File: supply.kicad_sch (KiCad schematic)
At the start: 57 parts, among them Q1 DMG1012T-7, Q3 DMG1012T-7, U1 AP62301_TSOT, U2 AP62301_TSOT, U3 NCP163ASN330T1G, U4 REF3012AIDBZT, U5 TLV73312PDBVT

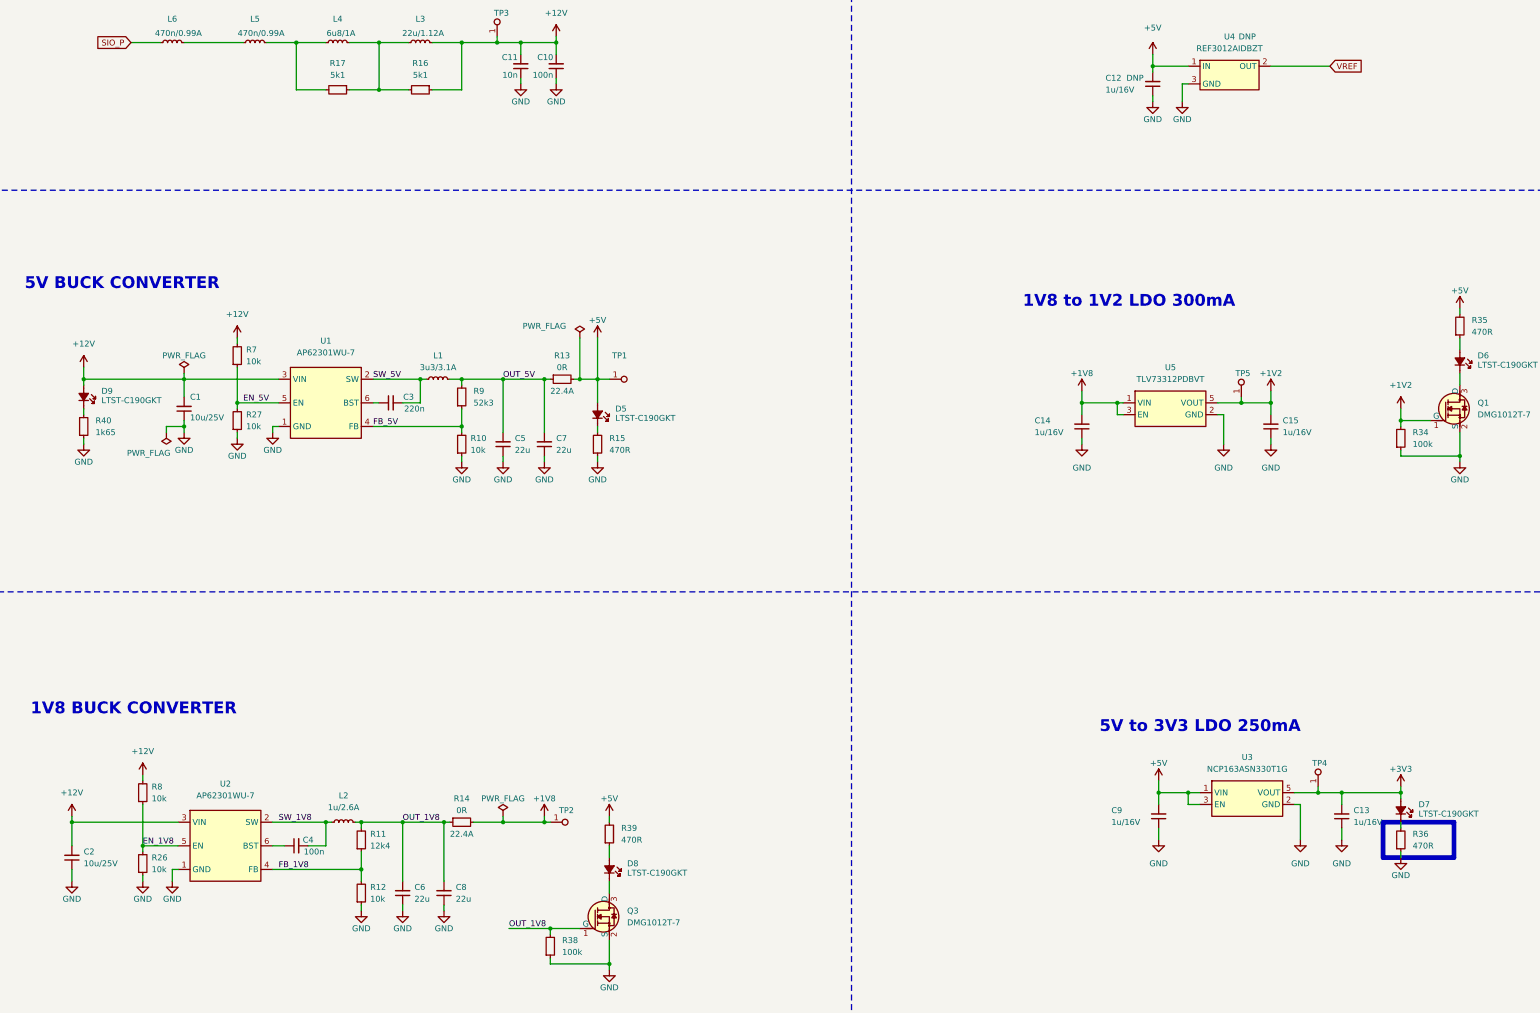
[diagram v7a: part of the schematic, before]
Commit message: [#55438] Place LED indicators on PCB
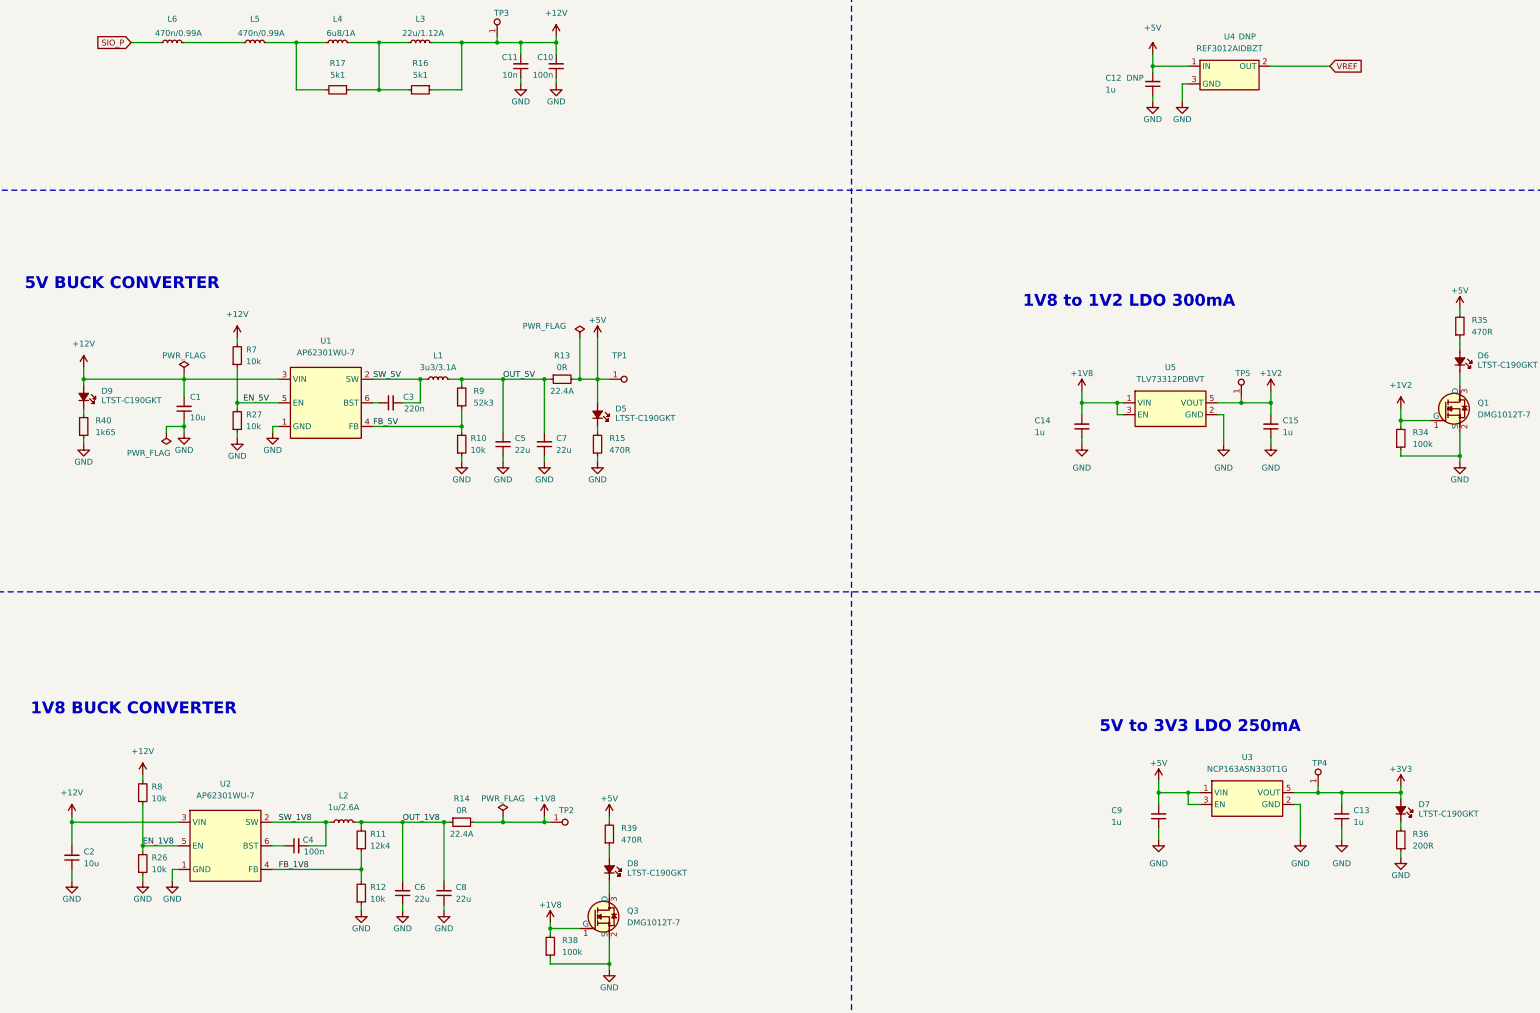
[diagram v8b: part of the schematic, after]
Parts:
- removed R36: R_470R_0402, antmicro-footprints:R_0402_1005Metric, symbol antmicroResistors0402:R_470R_0402
- added R36: R_200R_0402, antmicro-footprints:R_0402_1005Metric, symbol antmicroResistors0402:R_200R_0402
- C1, C2: Val 10u/25V -> 10u; Voltage (none) -> 25V
- C12, C13, C14, C15, C9: Val 1u/16V -> 1u; Voltage (none) -> 16V
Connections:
- net +1V8: now also Q3.1 (G), R38.2
- net GND: now also R36.1
- net OUT_1V8: no longer Q3.1 (G), R38.2
- net at D7.1 (C): now also R36.2
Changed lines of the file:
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@@
     (stroke (width 0) (type default))
   )
-  (wire (pts (xy 147.32 240.03) (xy 156.21 240.03))
-    (stroke (width 0) (type default))
-  )
   (wire (pts (xy 154.94 215.9) (xy 154.94 217.17))
     (stroke (width 0) (type default))
@@
     (stroke (width 0) (type default))
   )
+  (wire (pts (xy 156.21 238.76) (xy 156.21 240.03))
+    (stroke (width 0) (type default))
+  )
   (wire (pts (xy 101.6 49.53) (xy 107.95 49.53))
     (stroke (width 0) (type default))
@@
     (stroke (width 0) (type default))
   )
-  (rectangle (start 335.28 217.17) (end 350.52 224.79)
-    (stroke (width 1) (type default) (color 255 0 0 1))
-    (fill (type none))
-  )
   (image (at 35.56 274.32) (scale 0.4)
     (data
@@
     (effects (font (size 1.27 1.27)) (justify left bottom))
   )
-  (label "OUT_1V8" (at 147.32 240.03 0) (fields_autoplaced)
-    (effects (font (size 1.27 1.27)) (justify left bottom))
-  )
   (label "EN_5V" (at 90.17 127 0) (fields_autoplaced)
     (effects (font (size 1.27 1.27)) (justify left bottom))
@@
       (effects (font (size 1.27 1.27) (thickness 0.15)) (justify left bottom) hide)
     )
-    (property "Val" "1u/16V" (at 328.93 217.17 90)
+    (property "Val" "1u" (at 328.93 217.17 90)
       (effects (font (size 1.27 1.27) (thickness 0.15)) (justify right))
     )
-    (property "Voltage" "" (at 354.33 198.12 0)
+    (property "Voltage" "16V" (at 354.33 198.12 0)
       (effects (font (size 1.27 1.27)) (justify left bottom) hide)
     )
@@
       (effects (font (size 1.27 1.27) (thickness 0.15)) (justify left bottom) hide)
     )
-    (property "Val" "10u/25V" (at 55.88 226.0535 90)
+    (property "Val" "10u" (at 55.88 226.0535 90)
       (effects (font (size 1.27 1.27) (thickness 0.15)) (justify right))
     )
-    (property "Voltage" "" (at 81.28 207.01 0)
+    (property "Voltage" "25V" (at 81.28 207.01 0)
       (effects (font (size 1.27 1.27)) (justify left bottom) hide)
     )
@@
       (effects (font (size 1.27 1.27) (thickness 0.15)) (justify left bottom) hide)
     )
-    (property "Val" "1u/16V" (at 275.59 59.69 90)
+    (property "Val" "1u" (at 275.59 59.69 90)
       (effects (font (size 1.27 1.27) (thickness 0.15)) (justify right))
     )
-    (property "Voltage" "" (at 313.69 40.64 0)
+    (property "Voltage" "16V" (at 313.69 40.64 0)
       (effects (font (size 1.27 1.27)) (justify left bottom) hide)
     )
@@
     )
   )
+  (symbol (lib_id "antmicropower:+1V8") (at 156.21 238.76 0) (unit 1)
+    (in_bom yes) (on_board yes) (dnp no)
+    (property "Reference" "#PWR012" (at 171.45 241.3 0)
+      (effects (font (size 1.27 1.27) (thickness 0.15)) (justify left bottom) hide)
+    )
+    (property "Value" "+1V8" (at 156.21 234.95 0)
+      (effects (font (size 1.27 1.27) (thickness 0.15)))
+    )
+    (property "Footprint" "" (at 171.45 246.38 0)
+      (effects (font (size 1.27 1.27) (thickness 0.15)) (justify left bottom) hide)
+    )
+    (property "Datasheet" "" (at 171.45 248.92 0)
+      (effects (font (size 1.27 1.27) (thickness 0.15)) (justify left bottom) hide)
+    )
+    (property "Author" "Antmicro" (at 171.45 246.38 0)
+      (effects (font (size 1.27 1.27) (thickness 0.15)) (justify left bottom) hide)
+    )
+    (property "License" "Apache-2.0" (at 171.45 248.92 0)
+      (effects (font (size 1.27 1.27) (thickness 0.15)) (justify left bottom) hide)
+    )
+    (pin "1")
+    (instances
+      (project "gmsl-serializer"
+        (path "/dbd1044a-3803-4c19-8db2-96636cba7198/a0eea618-ebab-4bb8-b0df-45f61b300adb"
+          (reference "#PWR012") (unit 1)
+        )
+      )
+    )
+  )
   (symbol (lib_id "antmicroResistors0402:R_100k_0402") (at 339.09 137.16 90) (unit 1)
     (in_bom yes) (on_board yes) (dnp no) (fields_autoplaced)
@@
     )
   )
+  (symbol (lib_id "antmicroResistors0402:R_200R_0402") (at 339.09 223.52 270) (mirror x) (unit 1)
+    (in_bom yes) (on_board yes) (dnp no)
+    (property "Reference" "R36" (at 341.63 219.71 90)
+      (effects (font (size 1.27 1.27) (thickness 0.15)) (justify left))
+    )
+    (property "Value" "R_200R_0402" (at 326.39 203.2 0)
+      (effects (font (size 1.27 1.27) (thickness 0.15)) (justify left bottom) hide)
+    )
+    (property "Footprint" "antmicro-footprints:R_0402_1005Metric" (at 323.85 203.2 0)
+      (effects (font (size 1.27 1.27) (thickness 0.15)) (justify left bottom) hide)
+    )
+    (property "Datasheet" "https://www.bourns.com/docs/product-datasheets/cr.pdf" (at 321.31 203.2 0)
+      (effects (font (size 1.27 1.27) (thickness 0.15)) (justify left bottom) hide)
+    )
+    (property "MPN" "CR0402-FX-2000GLF" (at 318.77 203.2 0)
+      (effects (font (size 1.27 1.27) (thickness 0.15)) (justify left bottom) hide)
+    )
+    (property "Manufacturer" "Bourns" (at 316.23 203.2 0)
+      (effects (font (size 1.27 1.27) (thickness 0.15)) (justify left bottom) hide)
+    )
+    (property "License" "Apache-2.0" (at 313.69 203.2 0)
+      (effects (font (size 1.27 1.27) (thickness 0.15)) (justify left bottom) hide)
+    )
+    (property "Author" "Antmicro" (at 311.15 203.2 0)
+      (effects (font (size 1.27 1.27) (thickness 0.15)) (justify left bottom) hide)
+    )
+    (property "Val" "200R" (at 341.63 222.25 90)
+      (effects (font (size 1.27 1.27) (thickness 0.15)) (justify left))
+    )
+    (property "Tolerance" "1%" (at 328.93 203.2 0)
+      (effects (font (size 1.27 1.27)) (justify left bottom) hide)
+    )
+    (property "Public" "" (at 308.61 203.2 0)
+      (effects (font (size 1.27 1.27)) (justify left bottom) hide)
+    )
+    (pin "2")
+    (pin "1")
+    (instances
+      (project "gmsl-serializer"
+        (path "/dbd1044a-3803-4c19-8db2-96636cba7198/a0eea618-ebab-4bb8-b0df-45f61b300adb"
+          (reference "R36") (unit 1)
+        )
+      )
+    )
+  )
   (symbol (lib_id "antmicropower:+3V3") (at 339.09 209.55 0) (unit 1)
     (in_bom yes) (on_board yes) (dnp no)
@@
       (effects (font (size 1.27 1.27) (thickness 0.15)) (justify left bottom) hide)
     )
-    (property "Val" "1u/16V" (at 313.69 133.35 90)
+    (property "Val" "1u" (at 313.69 133.35 90)
       (effects (font (size 1.27 1.27) (thickness 0.15)) (justify right))
     )
-    (property "Voltage" "" (at 339.09 114.3 0)
+    (property "Voltage" "16V" (at 339.09 114.3 0)
       (effects (font (size 1.27 1.27)) (justify left bottom) hide)
     )
@@
     )
   )
-  (symbol (lib_id "antmicroResistors0402:R_470R_0402") (at 339.09 223.52 90) (unit 1)
-    (in_bom yes) (on_board yes) (dnp no) (fields_autoplaced)
-    (property "Reference" "R36" (at 341.63 219.7099 90)
-      (effects (font (size 1.27 1.27) (thickness 0.15)) (justify right))
-    )
-    (property "Value" "R_470R_0402" (at 351.79 203.2 0)
-      (effects (font (size 1.27 1.27) (thickness 0.15)) (justify left bottom) hide)
-    )
-    (property "Footprint" "antmicro-footprints:R_0402_1005Metric" (at 354.33 203.2 0)
-      (effects (font (size 1.27 1.27) (thickness 0.15)) (justify left bottom) hide)
-    )
-    (property "Datasheet" "https://www.bourns.com/docs/product-datasheets/cr.pdf" (at 356.87 203.2 0)
-      (effects (font (size 1.27 1.27) (thickness 0.15)) (justify left bottom) hide)
-    )
-    (property "MPN" "CR0402-FX-4700GLF" (at 359.41 203.2 0)
-      (effects (font (size 1.27 1.27) (thickness 0.15)) (justify left bottom) hide)
-    )
-    (property "Manufacturer" "Bourns" (at 361.95 203.2 0)
-      (effects (font (size 1.27 1.27) (thickness 0.15)) (justify left bottom) hide)
-    )
-    (property "License" "Apache-2.0" (at 364.49 203.2 0)
-      (effects (font (size 1.27 1.27) (thickness 0.15)) (justify left bottom) hide)
-    )
-    (property "Author" "Antmicro" (at 367.03 203.2 0)
-      (effects (font (size 1.27 1.27) (thickness 0.15)) (justify left bottom) hide)
-    )
-    (property "Val" "470R" (at 341.63 222.2499 90)
-      (effects (font (size 1.27 1.27) (thickness 0.15)) (justify right))
-    )
-    (property "Tolerance" "1%" (at 349.25 203.2 0)
-      (effects (font (size 1.27 1.27)) (justify left bottom) hide)
-    )
-    (pin "1")
-    (pin "2")
-    (instances
-      (project "gmsl-serializer"
-        (path "/dbd1044a-3803-4c19-8db2-96636cba7198/a0eea618-ebab-4bb8-b0df-45f61b300adb"
-          (reference "R36") (unit 1)
-        )
-      )
-    )
-  )
   (symbol (lib_id "antmicroTestPoints:TP_1.5mm_SMD") (at 144.78 48.26 270) (mirror x) (unit 1)
     (in_bom yes) (on_board yes) (dnp no)
@@
       (effects (font (size 1.27 1.27) (thickness 0.15)) (justify left bottom) hide)
     )
-    (property "Val" "1u/16V" (at 276.86 217.17 90)
+    (property "Val" "1u" (at 276.86 217.17 90)
       (effects (font (size 1.27 1.27) (thickness 0.15)) (justify right))
     )
-    (property "Voltage" "" (at 314.96 198.12 0)
+    (property "Voltage" "16V" (at 314.96 198.12 0)
       (effects (font (size 1.27 1.27)) (justify left bottom) hide)
     )
@@
       (effects (font (size 1.27 1.27) (thickness 0.15)) (justify left bottom) hide)
     )
-    (property "Val" "1u/16V" (at 260.35 133.35 90)
+    (property "Val" "1u" (at 260.35 133.35 90)
       (effects (font (size 1.27 1.27) (thickness 0.15)) (justify right))
     )
-    (property "Voltage" "" (at 298.45 114.3 0)
+    (property "Voltage" "16V" (at 298.45 114.3 0)
       (effects (font (size 1.27 1.27)) (justify left bottom) hide)
     )
@@
       (effects (font (size 1.27 1.27) (thickness 0.15)) (justify left bottom) hide)
     )
-    (property "Val" "10u/25V" (at 78.74 130.175 90)
+    (property "Val" "10u" (at 78.74 130.175 90)
       (effects (font (size 1.27 1.27) (thickness 0.15)) (justify right))
     )
-    (property "Voltage" "" (at 105.41 110.49 0)
+    (property "Voltage" "25V" (at 105.41 110.49 0)
       (effects (font (size 1.27 1.27)) (justify left bottom) hide)
     )
